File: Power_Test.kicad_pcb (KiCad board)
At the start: 2 copper layers, 72.7 x 75 mm, 52 parts, among them J1 Conn_01x01, J10 Conn_01x01, J11 Conn_01x01, J12 Conn_02x02_Odd_Even, J2 Conn_01x01, J3 Conn_01x01, J4 Conn_01x01, J5 Conn_02x05_Odd_Even, J6 Conn_02x05_Odd_Even, J7 Conn_02x02_Odd_Even, J8 Conn_01x01, J9 Conn_01x01, Q1 C2M0280120D, Q2 C2M0280120D, Q3 C2M0280120D, Q4 C2M0280120D, Q5 C2M0280120D, Q6 C2M0280120D, Q7 C2M0280120D, Q8 C2M0280120D

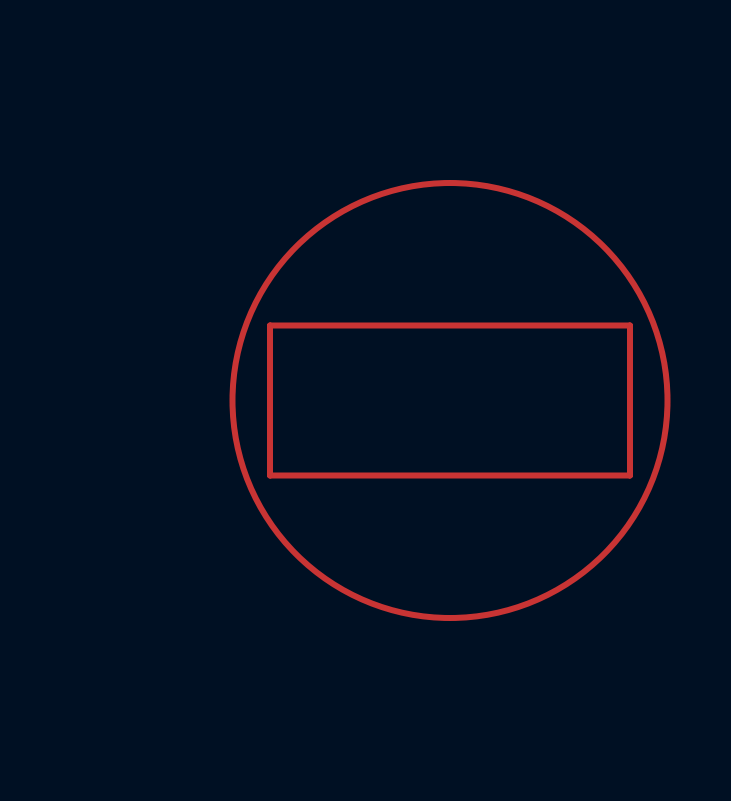
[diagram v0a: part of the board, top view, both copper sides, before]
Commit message: VER1.0: обновил компоновку и добавил чертеж шины
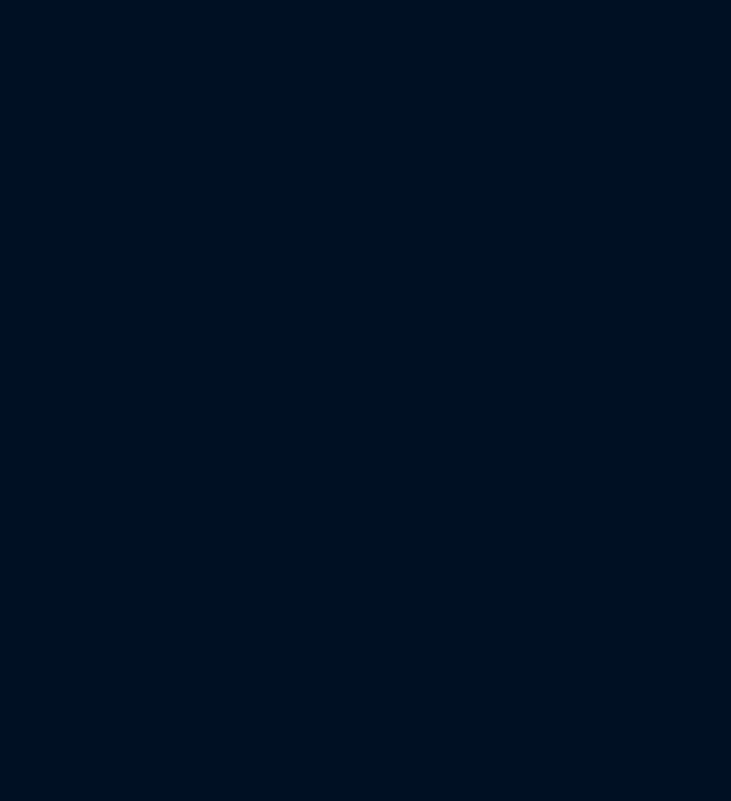
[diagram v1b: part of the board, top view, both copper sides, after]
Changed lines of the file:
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@@
 		(embedded_fonts no)
 		(model "${KIPRJMOD}/3D/Bus_copper_bottom.stp"
+			(hide yes)
 			(offset
 				(xyz -2.5 1.5 -0.1)
@@
 			)
 		)
+		(model "${KIPRJMOD}/3D/Bush_phase_mono.stp"
+			(offset
+				(xyz 2.5 -79 5)
+			)
+			(scale
+				(xyz 1 1 1)
+			)
+			(rotate
+				(xyz -90 180 90)
+			)
+		)
 	)
 	(footprint "Resistor_SMD:R_0805_2012Metric_Pad1.20x1.40mm_HandSolder"
@@
 		(embedded_fonts no)
 		(model "${KIPRJMOD}/3D/Bus_copper_top.stp"
+			(hide yes)
 			(offset
 				(xyz -2.5 -1.5 -1.4)
@@
 		)
 		(model "${KIPRJMOD}/3D/Curent_Sensor_Test.step"
+			(hide yes)
 			(offset
 				(xyz 0 64 12.5)
@@
 		)
 	)
-	(gr_circle
-		(center 283.25 133.25)
-		(end 283.25 126)
-		(stroke
-			(width 0.2)
-			(type default)
-		)
-		(fill no)
-		(layer "F.Cu")
-	)
-	(gr_rect
-		(start 277.25 130.75)
-		(end 289.25 135.75)
-		(stroke
-			(width 0.2)
-			(type default)
-		)
-		(fill no)
-		(layer "F.Cu")
-	)
 	(gr_line
 		(start 145.5 95.75)
@@
 	(dimension
 		(type orthogonal)
+		(layer "F.Mask")
+		(pts
+			(xy 185.75 160.5) (xy 185.75 95.75)
+		)
+		(height -49.5)
+		(orientation 1)
+		(format
+			(prefix "")
+			(suffix "")
+			(units 3)
+			(units_format 0)
+			(precision 4)
+			(suppress_zeroes yes)
+		)
+		(style
+			(thickness 0.1)
+			(arrow_length 1.27)
+			(text_position_mode 0)
+			(arrow_direction outward)
+			(extension_height 0.58642)
+			(extension_offset 0.5)
+			(keep_text_aligned yes)
+		)
+		(gr_text "64,75"
+			(at 135.1 128.125 90)
+			(layer "F.Mask")
+			(effects
+				(font
+					(size 1 1)
+					(thickness 0.15)
+				)
+			)
+		)
+	)
+	(dimension
+		(type orthogonal)
+		(layer "F.Mask")
+		(pts
+			(xy 177.75 95.75) (xy 185.75 95.75)
+		)
+		(height -3)
+		(orientation 0)
+		(format
+			(prefix "")
+			(suffix "")
+			(units 3)
+			(units_format 0)
+			(precision 4)
+			(suppress_zeroes yes)
+		)
+		(style
+			(thickness 0.1)
+			(arrow_length 1.27)
+			(text_position_mode 0)
+			(arrow_direction outward)
+			(extension_height 0.58642)
+			(extension_offset 0.5)
+			(keep_text_aligned yes)
+		)
+		(gr_text "8"
+			(at 181.75 91.6 0)
+			(layer "F.Mask")
+			(effects
+				(font
+					(size 1 1)
+					(thickness 0.15)
+				)
+			)
+		)
+	)
+	(dimension
+		(type orthogonal)
 		(layer "Edge.Cuts")
 		(pts
@@
 			)
 		)
+	)
+	(zone
+		(net 0)
+		(net_name "")
+		(layers "*.Mask")
+		(hatch none 0.5)
+		(connect_pads
+			(clearance 0.5)
+		)
+		(min_thickness 0.25)
+		(filled_areas_thickness no)
+		(fill yes
+			(thermal_gap 0.5)
+			(thermal_bridge_width 0.5)
+		)
+		(polygon
+			(pts
+				(xy 177.75 95.75) (xy 185.75 95.75) (xy 185.75 160.5) (xy 177.75 160.5)
+			)
+		)
